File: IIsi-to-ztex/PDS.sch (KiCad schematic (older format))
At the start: 28 parts, among them J2 650906-5, SW1 SW_SPDT, U1 SN74CB3T3245PWR, U10 SN74CB3T3245PWR, U11 SN74CB3T3245PWR, U13 SN74CB3T3245PWR, U2 SN74CB3T3245PWR, U3 SN74CB3T3245PWR, U4 SN74CB3T3245PWR, U5 SN74CB3T3245PWR, U6 SN74CB3T3245PWR, U7 SN74CB3T3245PWR, U8 SN74CB3T3245PWR, U9 SN74CB3T3245PWR

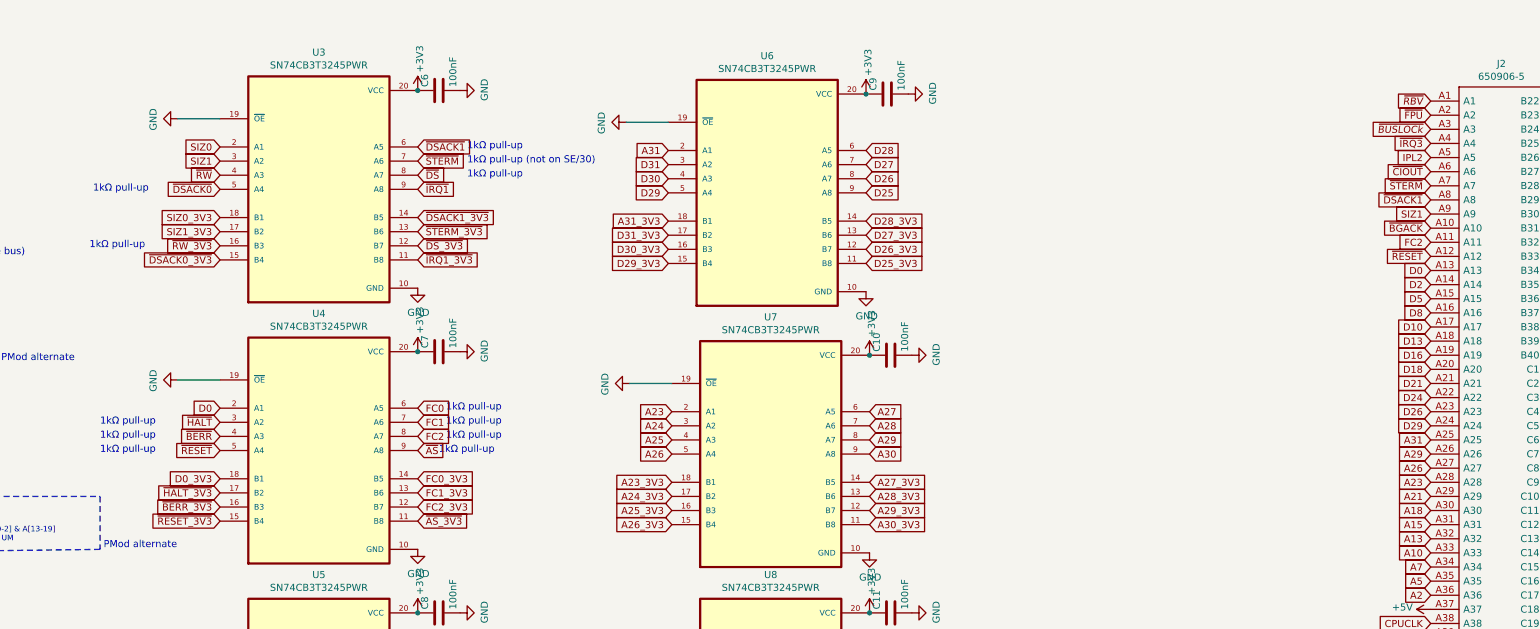
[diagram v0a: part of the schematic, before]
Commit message: rework /HALT
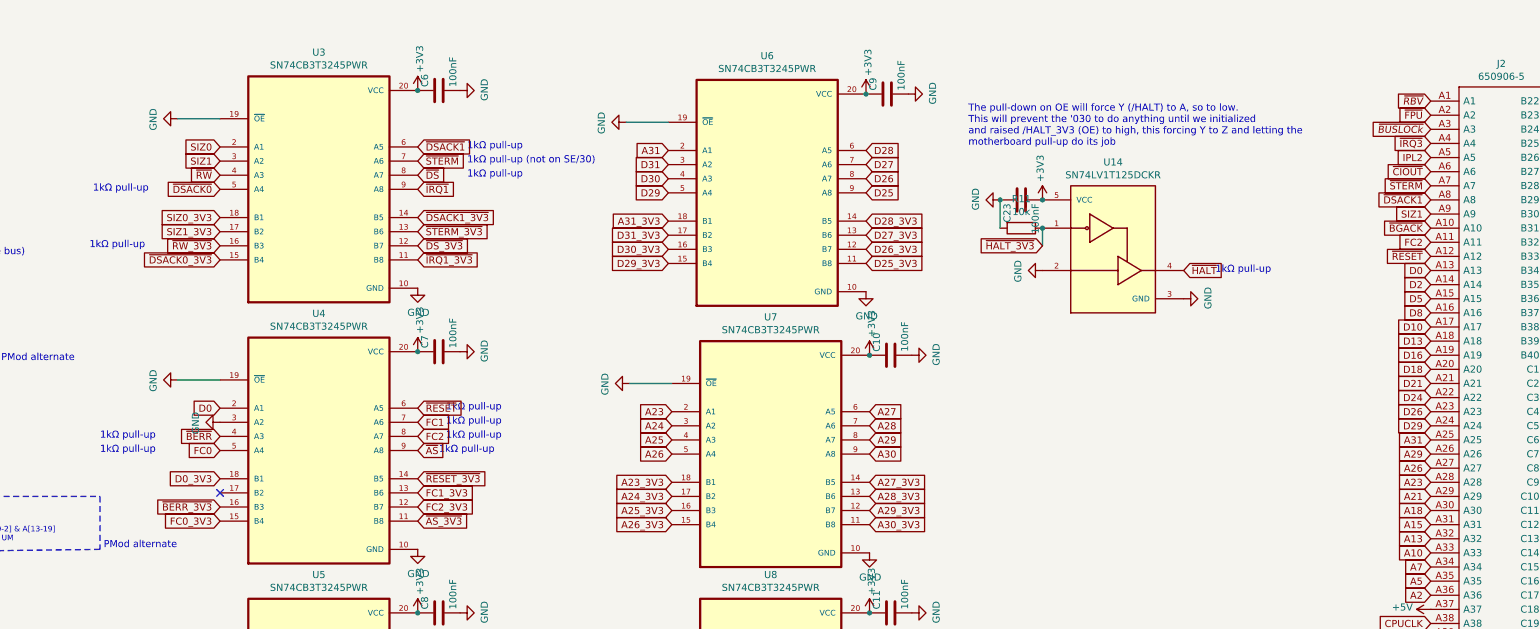
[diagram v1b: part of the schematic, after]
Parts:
- added C23: 100nF, Capacitor_SMD:C_0603_1608Metric, symbol Device:C
- added R11: 10k, Resistor_SMD:R_0603_1608Metric, symbol Device:R
- added U14: SN74LV1T125DCKR, For_SeeedStudio:SOT65P210X110-5N, symbol SN74LV1T125DCKR:SN74LV1T125DCKR
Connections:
- net +3V3: now also C23.2, U14.5 (VCC)
- net FC0: now also U4.5 (A4); no longer U4.6 (A5)
- net FC0_3V3: now also U4.15 (B4); no longer U4.14 (B5)
- net GND: now also U4.3 (A2), C23.1, R11.2, U14.2, U14.3 (GND)
- net ~HALT: now also U14.4; no longer U4.3 (A2)
- net ~HALT_3V3: now also R11.1, U14.1; no longer U4.17 (B2)
- net ~RESET: now also U4.6 (A5); no longer U4.5 (A4)
- net ~RESET_3V3: now also U4.14 (B5); no longer U4.15 (B4)
- no-connect marks 7 -> 8
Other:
- note added: "The pull-down on OE will force Y (/HALT) to A, so to low.\nThis will prevent the '030 to do anything until we initialized\nand raised /HALT_3V3 (OE) to high, this forcing Y to Z and letting the\nmotherboard pull-up do its job"
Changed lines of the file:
@@
 Text GLabel 2475 1750 2    50   Input ~ 0
 ~IRQ1
-Text GLabel 1075 3400 0    50   Input ~ 0
+Text GLabel 7900 2325 2    50   Input ~ 0
 ~HALT
 Text GLabel -1500 1300 0    50   Input ~ 0
@@
 Text GLabel 1075 1450 0    50   Input ~ 0
 SIZ0
-Text GLabel 1075 3600 0    50   Input ~ 0
+Text GLabel 2475 3300 2    50   Input ~ 0
 ~RESET
 Text GLabel 4250 1775 0    50   Input ~ 0
@@
 Text GLabel 2475 2150 2    50   Input ~ 0
 ~DS_3V3
-Text GLabel 1075 3900 0    50   Input ~ 0
+Text GLabel 6900 2150 0    50   Input ~ 0
 ~HALT_3V3
 Text GLabel 1075 3800 0    50   Input ~ 0
@@
 Text GLabel 1075 4000 0    50   Input ~ 0
 ~BERR_3V3
-Text GLabel 1075 4100 0    50   Input ~ 0
+Text GLabel 2475 3800 2    50   Input ~ 0
 ~RESET_3V3
 Connection ~ 2475 2900
@@
 Text GLabel 2475 3500 2    50   Input ~ 0
 FC2
-Text GLabel 2475 3300 2    50   Input ~ 0
+Text GLabel 1075 3600 0    50   Input ~ 0
 FC0
 Text GLabel 2475 3600 2    50   Input ~ 0
@@
 Text GLabel 2475 4000 2    50   Input ~ 0
 FC2_3V3
-Text GLabel 2475 3800 2    50   Input ~ 0
+Text GLabel 1075 4100 0    50   Input ~ 0
 FC0_3V3
 Text GLabel 2475 4100 2    50   Input ~ 0
@@
 Text Notes 2675 3525 0    50   ~ 0
  1kΩ pull-up
-Text Notes 225  3425 0    50   ~ 0
+Text Notes 8125 2350 0    50   ~ 0
  1kΩ pull-up
 Text Notes 225  3625 0    50   ~ 0
@@
 Text Notes 250  4300 0    50   ~ 0
 PMod alternate
+$Comp
+L power:+3V3 #PWR0135
+U 1 1 645A41EC
+P 6900 1825
+F 0 "#PWR0135" H 6900 1675 50  0001 C CNN
+F 1 "+3V3" V 6915 1953 50  0000 L CNN
+F 2 "" H 6900 1825 50  0001 C CNN
+F 3 "" H 6900 1825 50  0001 C CNN
+	1    6900 1825
+	-1   0    0    -1
+$EndComp
+$Comp
+L Device:C C?
+U 1 1 645A41FA
+P 6750 1825
+AR Path="/618F532C/645A41FA" Ref="C?"  Part="1"
+AR Path="/618E8C75/645A41FA" Ref="C?"  Part="1"
+AR Path="/631F3844/645A41FA" Ref="C?"  Part="1"
+AR Path="/631EF9BC/645A41FA" Ref="C?"  Part="1"
+AR Path="/6432B33E/645A41FA" Ref="C23"  Part="1"
+F 0 "C23" H 6775 1925 50  0000 L CNN
+F 1 "100nF" H 6775 1725 50  0000 L CNN
+F 2 "Capacitor_SMD:C_0603_1608Metric" H 6788 1675 50  0001 C CNN
+F 3 "" H 6750 1825 50  0000 C CNN
+F 4 "www.yageo.com" H 6750 1825 50  0001 C CNN "MNF1_URL"
+F 5 "CC0603KRX7R9BB104" H 6750 1825 50  0001 C CNN "MPN"
+F 6 "603-CC603KRX7R8BB104" H 6750 1825 50  0001 C CNN "Mouser"
+F 7 "?" H 6750 1825 50  0001 C CNN "Digikey"
+F 8 "?" H 6750 1825 50  0001 C CNN "LCSC"
+F 9 "?" H 6750 1825 50  0001 C CNN "Koncar"
+F 10 "TB" H 6750 1825 50  0001 C CNN "Side"
+F 11 "https://www.lcsc.com/product-detail/Multilayer-Ceramic-Capacitors-MLCC-SMD-SMT_YAGEO-CC0603KRX7R9BB104_C14663.html" H 6750 1825 50  0001 C CNN "URL"
+	1    6750 1825
+	0    -1   1    0
+$EndComp
+$Comp
+L power:GND #PWR0197
+U 1 1 645A4200
+P 6600 1825
+F 0 "#PWR0197" H 6600 1575 50  0001 C CNN
+F 1 "GND" H 6605 1652 50  0000 C CNN
+F 2 "" H 6600 1825 50  0001 C CNN
+F 3 "" H 6600 1825 50  0001 C CNN
+	1    6600 1825
+	0    1    -1   0
+$EndComp
+$Comp
+L power:GND #PWR0198
+U 1 1 645AF459
+P 7900 2525
+F 0 "#PWR0198" H 7900 2275 50  0001 C CNN
+F 1 "GND" H 7905 2352 50  0000 C CNN
+F 2 "" H 7900 2525 50  0001 C CNN
+F 3 "" H 7900 2525 50  0001 C CNN
+	1    7900 2525
+	0    -1   -1   0
+$EndComp
+$Comp
+L power:GND #PWR0199
+U 1 1 645B0FE4
+P 6900 2325
+F 0 "#PWR0199" H 6900 2075 50  0001 C CNN
+F 1 "GND" H 6905 2152 50  0000 C CNN
+F 2 "" H 6900 2325 50  0001 C CNN
+F 3 "" H 6900 2325 50  0001 C CNN
+	1    6900 2325
+	0    1    1    0
+$EndComp
+$Comp
+L SN74LV1T125DCKR:SN74LV1T125DCKR U14
+U 1 1 645B87B7
+P 7400 2225
+F 0 "U14" H 7400 2892 50  0000 C CNN
+F 1 "SN74LV1T125DCKR" H 7400 2801 50  0000 C CNN
+F 2 "For_SeeedStudio:SOT65P210X110-5N" H 7400 2225 50  0001 L BNN
+F 3 "" H 7400 2225 50  0001 L BNN
+F 4 "IPC-7351B" H 7400 2225 50  0001 L BNN "STANDARD"
+F 5 "1.1mm" H 7400 2225 50  0001 L BNN "MAXIMUM_PACKAGE_HEIGHT"
+F 6 "Texas Instruments" H 7400 2225 50  0001 L BNN "MANUFACTURER"
+F 7 "A" H 7400 2225 50  0001 L BNN "PARTREV"
+F 8 "SN74LV1T125DCKR" H 7400 2225 50  0001 C CNN "MPN"
+	1    7400 2225
+	1    0    0    -1
+$EndComp
+$Comp
+L Device:R R11
+U 1 1 645D4516
+P 6750 2025
+F 0 "R11" V 6543 2025 50  0000 C CNN
+F 1 "10k" V 6634 2025 50  0000 C CNN
+F 2 "Resistor_SMD:R_0603_1608Metric" V 6680 2025 50  0001 C CNN
+F 3 "~" H 6750 2025 50  0001 C CNN
+F 4 "0603WAF1002T5E" V 6750 2025 50  0001 C CNN "MPN"
+	1    6750 2025
+	0    1    1    0
+$EndComp
+Connection ~ 6900 1825
+Wire Wire Line
+	6600 2025 6600 1825
+Connection ~ 6600 1825
+Wire Wire Line
+	6900 2150 6900 2025
+Connection ~ 6900 2025
+Text Notes 6375 1450 0    50   ~ 0
+The pull-down on OE will force Y (/HALT) to A, so to low.\nThis will prevent the '030 to do anything until we initialized\nand raised /HALT_3V3 (OE) to high, this forcing Y to Z and letting the\nmotherboard pull-up do its job
+$Comp
+L power:GND #PWR?
+U 1 1 646E2198
+P 1075 3400
+F 0 "#PWR?" H 1075 3150 50  0001 C CNN
+F 1 "GND" H 1080 3227 50  0000 C CNN
+F 2 "" H 1075 3400 50  0001 C CNN
+F 3 "" H 1075 3400 50  0001 C CNN
+	1    1075 3400
+	0    1    1    0
+$EndComp
+NoConn ~ 1075 3900
 $EndSCHEMATC

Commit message: cleanup DRC
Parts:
- removed SW1: SW_SPDT, For_SeeedStudio:CJS-1201B, symbol Switch:SW_SPDT
- added S1: SSAJ110100, For_SeeedStudio:SW_SSAJ110100, symbol SSAJ110100:SSAJ110100
- J2: DNP (none) -> DNP
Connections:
- net GND: no longer U13.3 (A2), U13.7 (A6)
- net ~IRQ2: now also U13.3 (A2)
- net ~IRQ3: now also U13.7 (A6)
- net ~MASTER_OE: now also S1.C
- net at R14.2: now also S1.2
- net at R15.2: now also S1.1
- net ~IRQ3_3V3: now reaches U13.13 (B6)
- net ~IRQ2_3V3: now reaches U13.17 (B2)
- no-connect marks 8 -> 6
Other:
- note added: "Not well documented... 40 MHZ clock on IIsi?\n(ECS on IIfx, RSVD on PDS)"
- note added: "Used for some cache signals (DCDMF3 p361) as well...\nHopefully not needed if the cache is filtering by addresses?"
- note added: "We won't do stand-alone FPU ?\n(~PDS.MASTER~ on IIfx, RSVD on PDS)"
- note added: "When ~MASTER_OE~ is low, this is enabled and various signals for Master & the extra clock (primary clock on IIfx) are available to the FPGA.\nWhen ~MASTER_OE~ is high, this is high-Z and the PMod can be used instead"
- note removed: "Not weel documented... 40 MHZ clock on IIsi?\n(ECS on IIfx, RSVD on PDS)"
- note removed: "We won't do stand-alone FPU\n(~PDS.MASTER~ on IIfx, RSVD on PDS)"
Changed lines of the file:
@@
 F 12 "650906-5" H 9650 1125 50  0001 C CNN "MPN"
 F 13 "https://www.lcsc.com/product-detail/Mezzanine-Connectors-Board-to-Board_TE-Connectivity-650906-5_C3652939.html" H 9650 1125 50  0001 C CNN "URL"
+F 14 "DNP" H 9650 1125 50  0001 C CNN "DNP"
 	1    9650 1125
 	1    0    0    -1
@@
 Text GLabel -3550 2950 0    50   Input Italic 0
 VIACLK
-Text GLabel -1500 5725 0    50   Input Italic 0
+Text GLabel -1500 6125 0    50   Input Italic 0
 ~PFW
 Text GLabel 6375 -1250 0    50   Input ~ 0
@@
 Text GLabel 4275 7300 0    50   Input ~ 0
 A10
-Text GLabel -1475 5325 0    50   Input ~ 0
+Text GLabel -1475 5725 0    50   Input ~ 0
 ~IRQ2
-Text GLabel -1475 5175 0    50   Input ~ 0
+Text GLabel -1475 5575 0    50   Input ~ 0
 ~IRQ3
 Text GLabel -1475 3625 0    50   Input Italic 0
@@
 Unused inputs to VIA2\n(~PDS.BR~, ~PDS.BG~ on IIfx)
 Text Notes -1725 4100 0    50   ~ 0
-We won't do stand-alone FPU\n(~PDS.MASTER~ on IIfx, RSVD on PDS)
+We won't do stand-alone FPU ?\n(~PDS.MASTER~ on IIfx, RSVD on PDS)
 Text Notes -1700 4625 0    50   ~ 0
 Access to IIsi internal video\n(GND on IIfx, RSVD on PDS)
-Text Notes -1725 5075 0    50   ~ 0
+Text Notes -1725 5475 0    50   ~ 0
 Extra IRQ\n(IRQ15 and RSVD on IIfx)
 Text Notes -3875 2825 0    50   ~ 0
 VIACLK on IIsi, ECLK on PDS, RSVD on IIfx\nECLK and VIACLK seem to be the same
-Text Notes -1725 5600 0    50   ~ 0
+Text Notes -1725 6000 0    50   ~ 0
 power failure
 Text Notes -3875 3400 0    50   ~ 0
-Not weel documented... 40 MHZ clock on IIsi?\n(ECS on IIfx, RSVD on PDS)
+Not well documented... 40 MHZ clock on IIsi?\n(ECS on IIfx, RSVD on PDS)
 Text GLabel 1075 2150 0    50   Input ~ 0
 ~RW_3V3
@@
 /FPU might be re-creatable from FC|0-2] & A[13-19]\nsee section 10.3 in the 68881/68882 UM
 $Comp
-L Switch:SW_SPDT SW1
-U 1 1 646843DE
-P 11850 -825
-F 0 "SW1" H 11850 -540 50  0000 C CNN
-F 1 "SW_SPDT" H 11850 -631 50  0000 C CNN
-F 2 "For_SeeedStudio:CJS-1201B" H 11850 -825 50  0001 C CNN
-F 3 "~" H 11850 -825 50  0001 C CNN
-F 4 "CJS-1201TB" H 11850 -825 50  0001 C CNN "MPN"
-	1    11850 -825
-	1    0    0    -1
-$EndComp
-$Comp
 L power:GND #PWR0127
 U 1 1 6468D0EA
@@
 Text GLabel 8975 -1425 0    50   Input ~ 0
 ~MASTER_OE
-Text GLabel 11650 -825 0    50   Input ~ 0
+Text GLabel 12050 -825 2    50   Input ~ 0
 ~MASTER_OE
 Text GLabel 10375 -1225 2    50   Input ~ 0
@@
 Text GLabel 10375 -425 2    50   Input ~ 0
 ~FPU_3V3
-$Comp
-L power:GND #PWR0138
-U 1 1 646A7A85
-P 10375 -1125
-F 0 "#PWR0138" H 10375 -1375 50  0001 C CNN
-F 1 "GND" H 10380 -1298 50  0000 C CNN
-F 2 "" H 10375 -1125 50  0001 C CNN
-F 3 "" H 10375 -1125 50  0001 C CNN
-	1    10375 -1125
-	0    -1   -1   0
-$EndComp
-$Comp
-L power:GND #PWR0142
-U 1 1 646A7E11
-P 8975 -1125
-F 0 "#PWR0142" H 8975 -1375 50  0001 C CNN
-F 1 "GND" H 8980 -1298 50  0000 C CNN
-F 2 "" H 8975 -1125 50  0001 C CNN
-F 3 "" H 8975 -1125 50  0001 C CNN
-	1    8975 -1125
-	0    1    1    0
-$EndComp
 NoConn ~ 8975 -425
-NoConn ~ 8975 -625
-NoConn ~ 10375 -625
 $Comp
 L Device:R R14
@@
 Text GLabel 10375 -1025 2    50   Input ~ 0
 C16M
-$Comp
-L power:GND #PWR0146
-U 1 1 6478CB98
-P 8975 -925
-F 0 "#PWR0146" H 8975 -1175 50  0001 C CNN
-F 1 "GND" H 8980 -1098 50  0000 C CNN
-F 2 "" H 8975 -925 50  0001 C CNN
-F 3 "" H 8975 -925 50  0001 C CNN
-	1    8975 -925
-	0    1    1    0
-$EndComp
 Text GLabel 10375 -525 2    50   Input ~ 0
 C16M_3V3
@@
 The pull-down on OE will force Y (/HALT) to A, so to low.\nThis will prevent the '030 to do anything until we initialized\nand raised /HALT_3V3 (OE) to high, this forcing Y to Z and letting the\nmotherboard pull-up do its job
 $Comp
-L power:GND #PWR?
+L power:GND #PWR0138
 U 1 1 646E2198
 P 1075 3400
-F 0 "#PWR?" H 1075 3150 50  0001 C CNN
+F 0 "#PWR0138" H 1075 3150 50  0001 C CNN
 F 1 "GND" H 1080 3227 50  0000 C CNN
 F 2 "" H 1075 3400 50  0001 C CNN
@@
 $EndComp
 NoConn ~ 1075 3900
+Wire Notes Line
+	-1750 5325 -1750 5825
+Wire Notes Line
+	-1750 5825 -725 5825
+Wire Notes Line
+	-725 5825 -725 5325
+Wire Notes Line
+	-725 5325 -1750 5325
+Text GLabel 10375 -1125 2    50   Input ~ 0
+~IRQ3
+Text GLabel 8975 -625 0    50   Input ~ 0
+~IRQ2_3V3
+Text GLabel 10375 -625 2    50   Input ~ 0
+~IRQ3_3V3
+$Comp
+L power:GND #PWR0142
+U 1 1 646A7E11
+P 8975 -925
+F 0 "#PWR0142" H 8975 -1175 50  0001 C CNN
+F 1 "GND" H 8980 -1098 50  0000 C CNN
+F 2 "" H 8975 -925 50  0001 C CNN
+F 3 "" H 8975 -925 50  0001 C CNN
+	1    8975 -925
+	0    1    1    0
+$EndComp
+Text GLabel 8975 -1125 0    50   Input ~ 0
+~IRQ2
+Text Notes -700 5825 0    50   ~ 0
+PMod alternate
+Text Notes -2150 4975 0    50   Italic 0
+Used for some cache signals (DCDMF3 p361) as well...\nHopefully not needed if the cache is filtering by addresses?
+$Comp
+L SSAJ110100:SSAJ110100 S1
+U 1 1 644C618A
+P 11950 -825
+F 0 "S1" H 11927 -1139 50  0000 C CNN
+F 1 "SSAJ110100" H 11927 -1048 50  0000 C CNN
+F 2 "For_SeeedStudio:SW_SSAJ110100" H 11950 -825 50  0001 L BNN
+F 3 "" H 11950 -825 50  0001 L BNN
+F 4 "0.9 mm" H 11950 -825 50  0001 L BNN "MAXIMUM_PACKAGE_HEIGHT"
+F 5 "ALPS" H 11950 -825 50  0001 L BNN "MANUFACTURER"
+F 6 "SSAJ110100" H 11950 -825 50  0001 L BNN "MPN"
+	1    11950 -825
+	-1   0    0    1
+$EndComp
+Text Notes 8650 -2050 0    50   ~ 0
+When ~MASTER_OE~ is low, this is enabled and various signals for Master & the extra clock (primary clock on IIfx) are available to the FPGA.\nWhen ~MASTER_OE~ is high, this is high-Z and the PMod can be used instead
 $EndSCHEMATC

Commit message: 3V3 SRAM draft
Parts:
- added C31: 1uF, Capacitor_SMD:C_0402_1005Metric, symbol Device:C
- C14, C16, C17, C18, C19, C20, C21, C22, C23, C4, C5, C6, C7: footprint Capacitor_SMD:C_0603_1608Metric -> Capacitor_SMD:C_0402_1005Metric; LCSC ? -> (none); MNF1_URL www.yageo.com -> (none); MPN CC0603KRX7R9BB104 -> CL05B104KO5NNNC; Mouser 603-CC603KRX7R8BB104 -> (none); URL https://www.lcsc.com/product-detail/Multilayer-Ceramic-Capa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 -> (none)
- R11, R14, R15: footprint Resistor_SMD:R_0603_1608Metric -> Resistor_SMD:R_0402_1005Metric; MPN 0603WAF1002T5E -> 0402WGF1002TCE
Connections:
- net +3V3: now also C31.1
- net C16M: no longer U13.8 (A7)
- net GND: now also C31.2; no longer U13.5 (A4)
- net ~BG: no longer U13.4 (A3)
- net ~BGACK: no longer U13.2 (A1)
- net ~BR: no longer U13.6 (A5)
- net ~FPU: no longer U13.9 (A8)
- net ~IRQ2: no longer U13.3 (A2)
- net ~IRQ3: no longer U13.7 (A6)
- net ~RBV: now also U13.9 (A8)
- net PMOD-78-: now reaches U13.15 (B4)
- net C16M_3V3 renamed PMOD-910-
- net ~BGACK_3V3 renamed PMOD-910+
- net ~BG_3V3 renamed PMOD-1112-
- net ~BR_3V3 renamed PMOD-1112+
- net ~FPU_3V3 renamed PMOD-78+
- net ~IRQ2_3V3 renamed PMOD-56-
- net ~IRQ3_3V3 renamed PMOD-56+
- net ~MASTER_OE renamed CACHE_~CE
- new net SRAM_A2: U13.6 (A5)
- new net SRAM_A3: U13.5 (A4)
- new net SRAM_B0_~WE: U13.8 (A7)
- new net SRAM_B1_~WE: U13.7 (A6)
- new net SRAM_B2_~WE: U13.3 (A2)
- new net SRAM_B3_~WE: U13.2 (A1)
- new net SRAM_~OE: U13.4 (A3)
- no-connect marks 6 -> 5
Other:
- note removed: "PMod alternate"
